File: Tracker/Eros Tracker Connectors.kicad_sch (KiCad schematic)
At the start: 13 parts, among them J1 2171790001, J2 S8B-PH-SM4-TB(LF)(SN), J3 S2B-PH-SM4-TB(LF)(SN), J4 24881, J5 24881, J6 24881, J7 24881

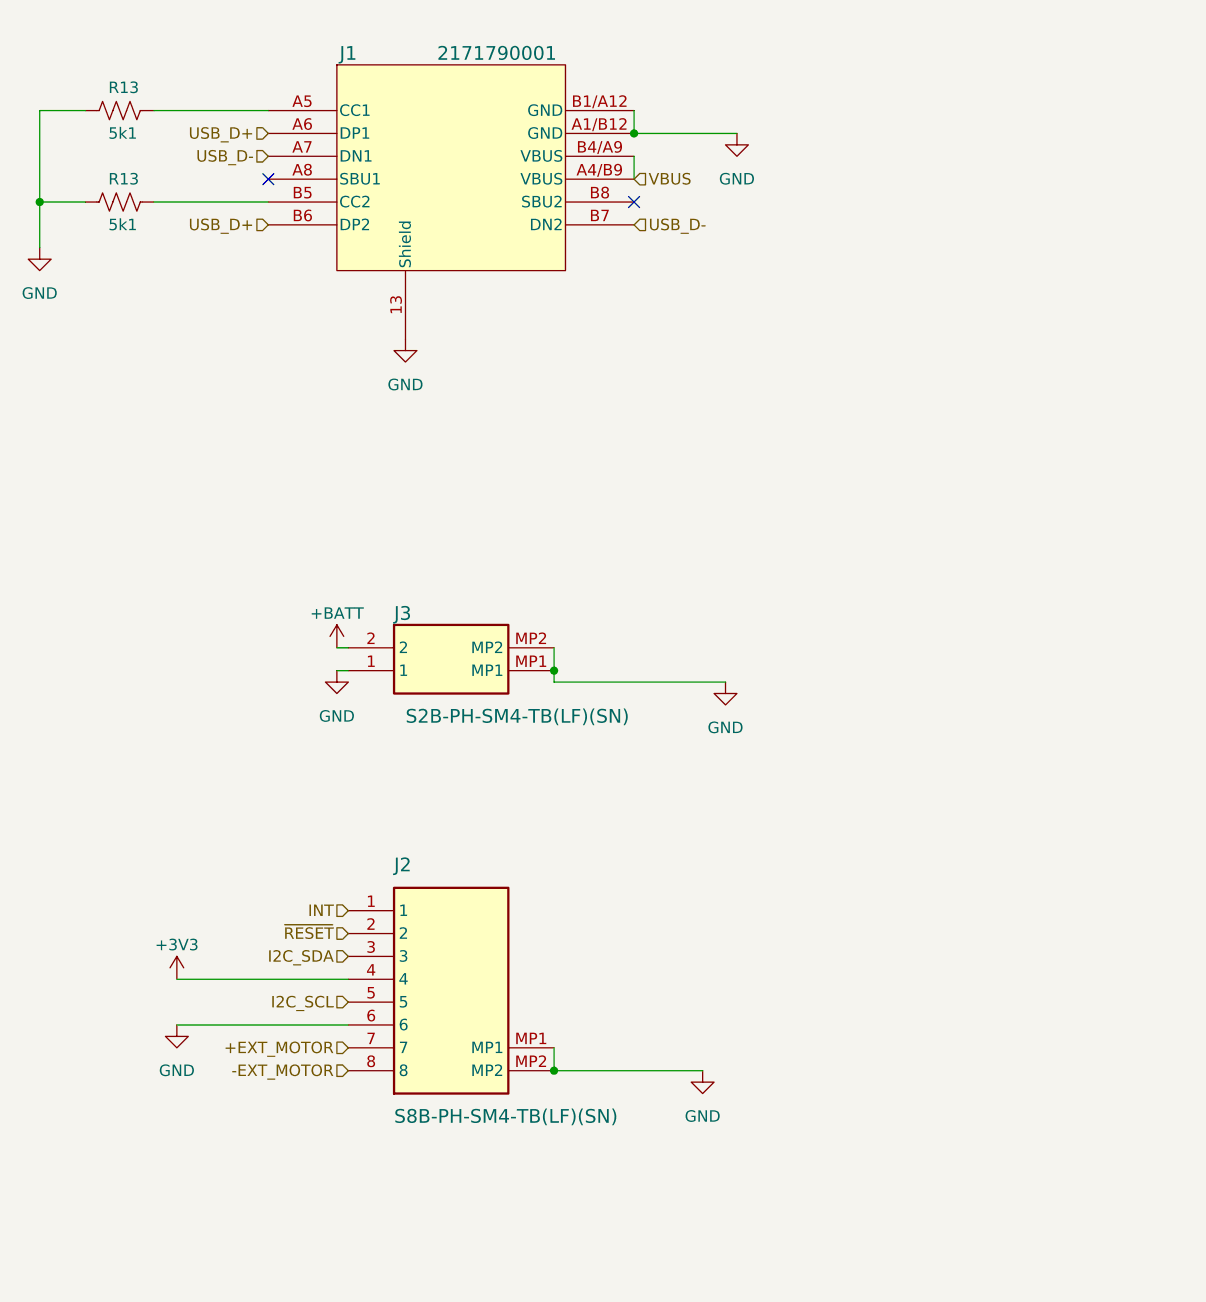
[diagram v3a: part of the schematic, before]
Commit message: RevC release. Power passthrough, battery voltage monitoring, IMU interrupt line fixed. TVS diodes added to all human-reachable connections.
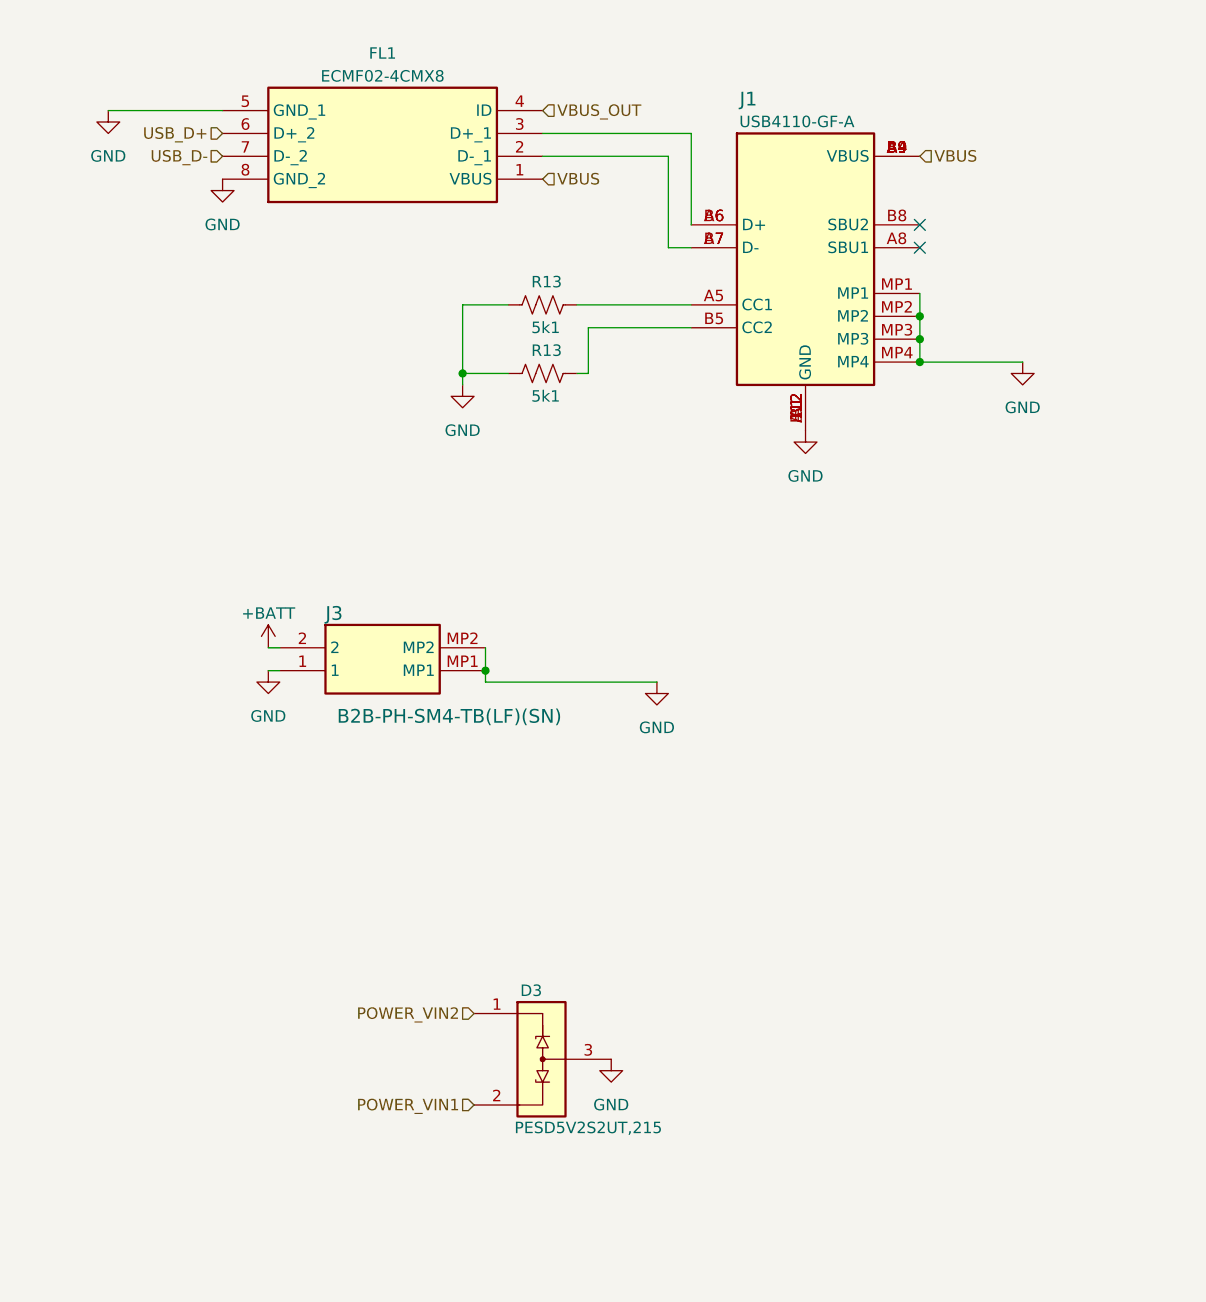
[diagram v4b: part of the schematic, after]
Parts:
- removed J2: S8B-PH-SM4-TB(LF)(SN), Eros Tracker:S8BPHSM4TBLFSN, symbol Eros Tracker:S8B-PH-SM4-TB_LF__SN_
- added D3: PESD5V2S2UT,215, Eros Tracker:SOT95P230X110-3N, symbol Eros Tracker:PESD5V2S2UT,215
- added FL1: ECMF02-4CMX8, Eros Tracker:ECMF024CMX8, symbol Eros Tracker:ECMF02-4CMX8
- J1: value 2171790001 -> USB4110-GF-A; footprint 2171790001_MOL -> Eros Tracker:USB4110GFA; symbol Eros Tracker:2171790001 -> Eros Tracker:USB4110-GF-A; Height (none) -> 3.26; Manufacturer_Name (none) -> GCT (GLOBAL CONNECTOR TECHNOLOGY); Manufacturer_Part_Number (none) -> USB4110-GF-A; Mouser Part Number (none) -> 640-USB4110-GF-A; Mouser Price/Stock (none) -> https://www.mouser.co.uk/ProductDetail/GCT/USB4110-GF-A?qs=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
- J3: value S2B-PH-SM4-TB(LF)(SN) -> B2B-PH-SM4-TB(LF)(SN); footprint Eros Tracker:S2BPHSM4TBLFSN -> Eros Tracker:B2BPHSM4TBLFSN; DigiKey Part Number (none) -> 455-B2B-PH-SM4-TBCT-ND; DigiKey Price/Stock (none) -> https://www.digikey.com/en/products/detail/jst-sales-americ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; Manufacturer_Part_Number S2B-PH-SM4-TB(LF)(SN) -> B2B-PH-SM4-TB(LF)(SN)
- R13: footprint Resistor_SMD:R_0805_2012Metric -> Resistor_SMD:R_0402_1005Metric; Manufacturer_Part_Number RT0805FRE135K1L -> RT0402FRE075K1L; Mouser Part Number 603-RT0805FRE135K1L -> 603-RT0402FRE075K1L; Mouser Price/Stock https://www.mouser.com/ProductDetail/YAGEO/RT0805FRE135K1L?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 -> https://www.mouser.com/ProductDetail/YAGEO/RT0402FRE075K1L?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
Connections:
- net GND: now also J1.A1 (GND), J1.A12 (GND), J1.B1 (GND), J1.B12 (GND), J1.MP1, J1.MP2, J1.MP3, J1.MP4, D3.3, FL1.12, FL1.5 (GND_1), FL1.8 (GND_2), FL1.9; no longer J1.13 (Shield), J1.14 (Shield), J1.15 (Shield), J1.16 (Shield), J1.A1/B12 (GND), J1.B1/A12 (GND)
- net POWER_VIN1: now also D3.2
- net POWER_VIN2: now also D3.1
- net USB_D+: now also FL1.6 (D+_2); no longer J1.A6 (DP1), J1.B6 (DP2)
- net USB_D-: now also FL1.7 (D-_2); no longer J1.A7 (DN1), J1.B7 (DN2)
- net VBUS: now also J1.A4 (VBUS), J1.A9 (VBUS), J1.B4 (VBUS), J1.B9 (VBUS), FL1.1 (VBUS), FL1.10; no longer J1.A4/B9 (VBUS), J1.B4/A9 (VBUS)
- net VBUS_OUT: now also FL1.11, FL1.4 (ID)
- new net: FL1.2 (D-_1), J1.A7 (D-), J1.B7 (D-)
- new net: FL1.3 (D+_1), J1.A6 (D+), J1.B6 (D+)
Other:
- moved on the sheet: J3, R13
